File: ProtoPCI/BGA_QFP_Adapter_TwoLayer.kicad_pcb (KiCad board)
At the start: 2 copper layers, 30.2 x 30.2 mm, 2 parts

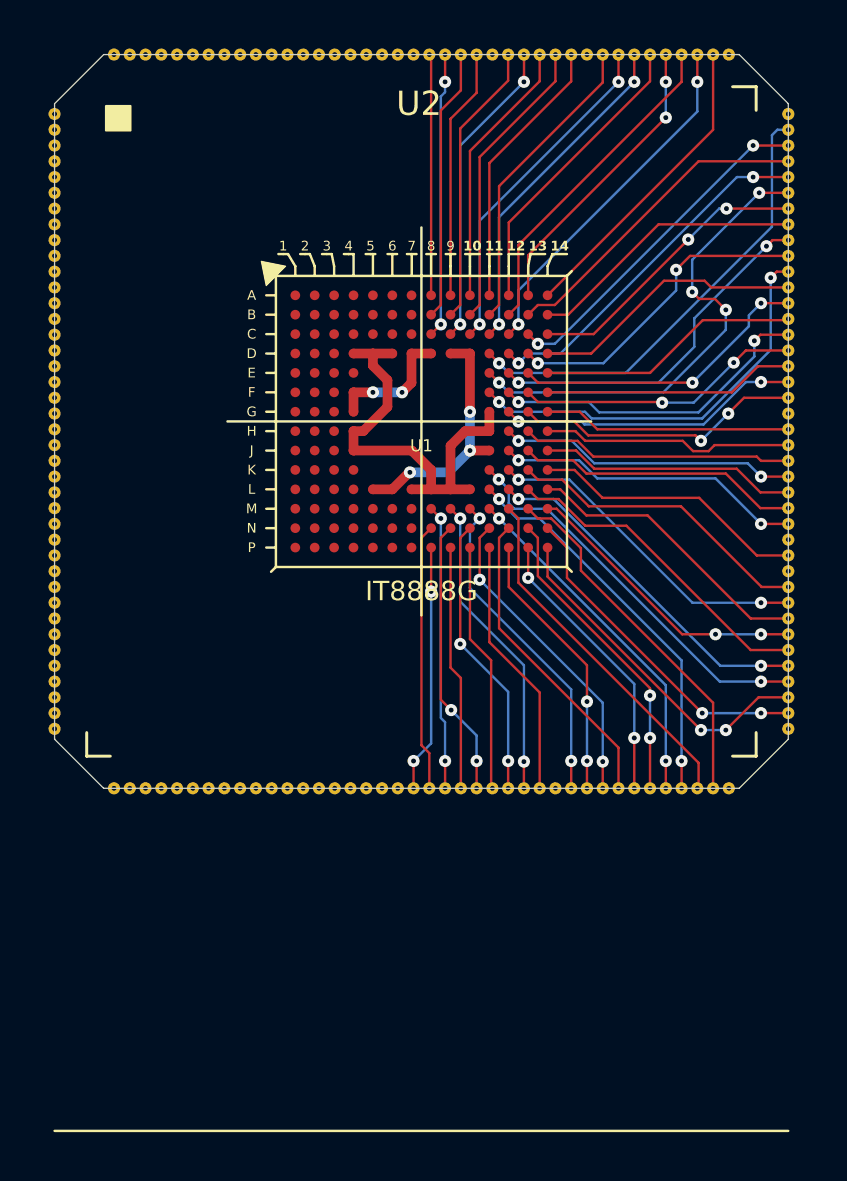
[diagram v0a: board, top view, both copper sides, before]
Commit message: BGA/QFP Adapter Two Layer Baseline
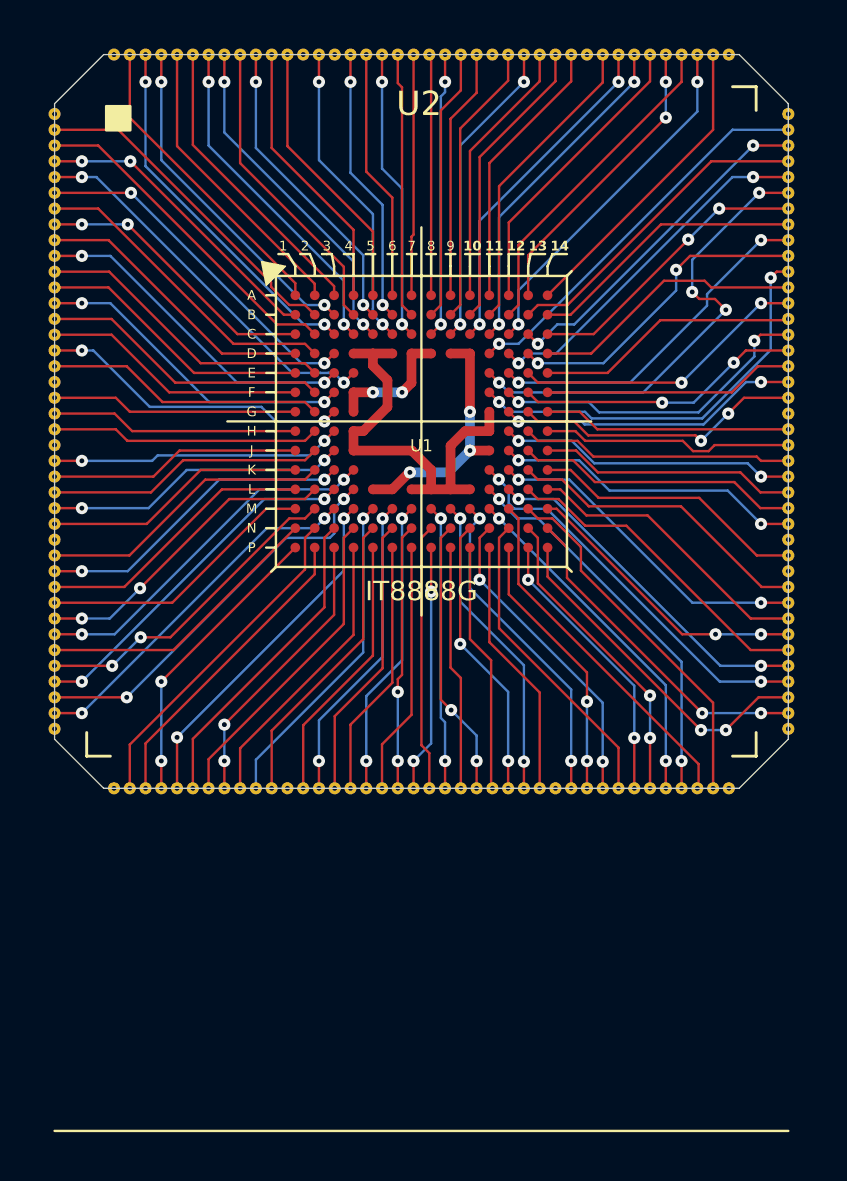
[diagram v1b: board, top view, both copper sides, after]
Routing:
- net Net-(U1-DACK5#): track 0.00 -> 16.4 mm, vias 0 -> 2
- net Net-(U1-TRDY#): track 0.00 -> 16.0 mm, vias 0 -> 2
- net Net-(U1-AD17): track 0.00 -> 15.2 mm, vias 0 -> 2
- net Net-(U1-SCLK): track 0.00 -> 15.1 mm, vias 0 -> 2
- net Net-(U1-DACK3#): track 0.00 -> 15.0 mm, vias 0 -> 2
- net Net-(U1-DACK6#): track 0.00 -> 14.8 mm, vias 0 -> 2
- net Net-(U1-DEVSEL#): track 0.00 -> 14.5 mm, vias 0 -> 2
- net Net-(U1-DRQ7): track 0.00 -> 14.5 mm, vias 0 -> 2
- net Net-(U1-AD18): track 0.00 -> 14.1 mm, vias 0 -> 2
- net Net-(U1-AD22): track 0.00 -> 14.0 mm, vias 0 -> 2
- net Net-(U1-AD21): track 0.00 -> 13.9 mm, vias 0 -> 2
- net Net-(U1-C/BE2#): track 0.00 -> 13.9 mm
- net Net-(U1-FRAME#): track 0.00 -> 13.9 mm
- net Net-(U1-DACK2#): track 0.00 -> 13.8 mm
- net Net-(U1-SERR#): track 0.00 -> 13.8 mm, vias 0 -> 2
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
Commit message: Finalized BGA/QFP Adapter (TwoLayer File *4LayerActual)
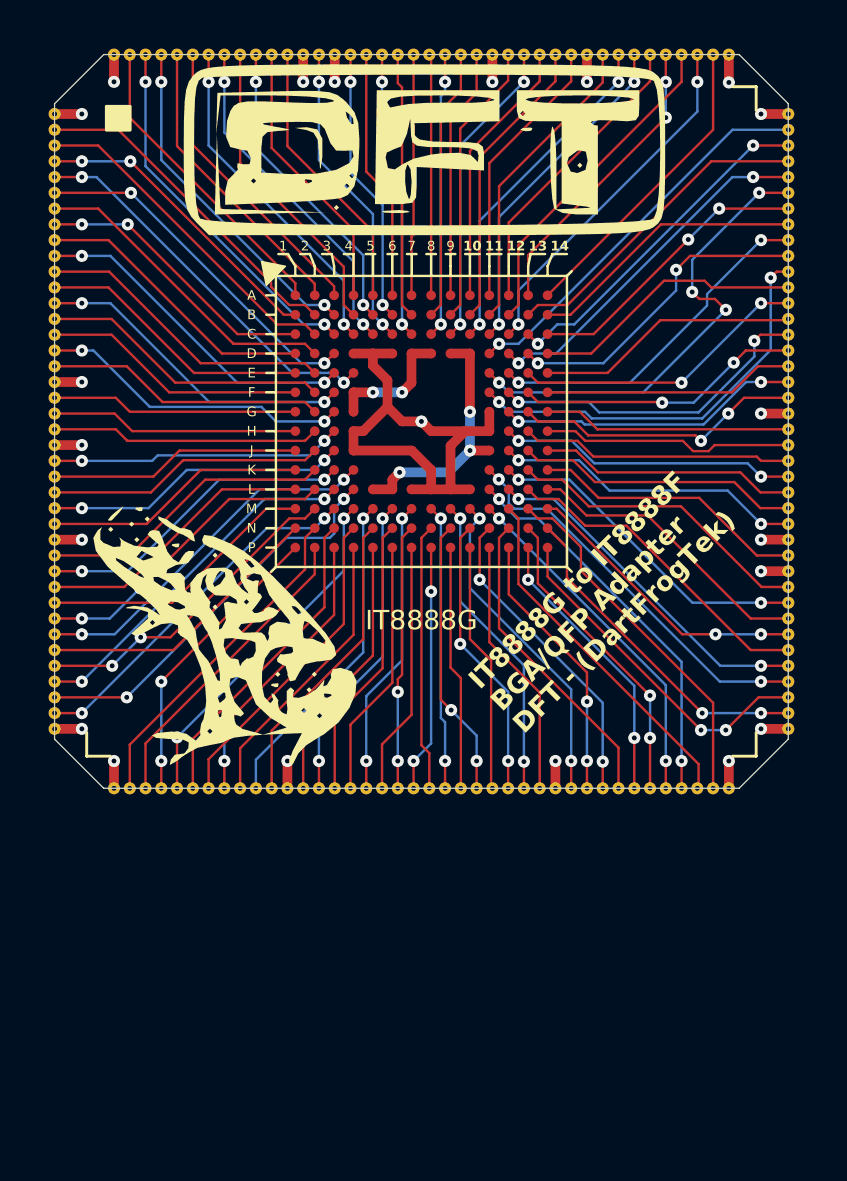
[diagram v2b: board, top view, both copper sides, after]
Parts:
- added G***: LOGO, ISA8888:DFT_Logo_Tiny, F.Cu at (166.7, 104.2)
- added G***: LOGO, ISA8888:DF_SS_Tiny, F.Cu at (158.5, 124.3)
- added G***: LOGO, ISA8888:DFT_SS_Small, B.Cu at (166.7, 115.0)
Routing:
- net /GND: track 17.9 -> 194.0 mm, vias 0 -> 13
- net /VCC: track 10.3 -> 83.9 mm, vias 3 -> 7
- net /VCC3: track 5.37 -> 61.9 mm, vias 2 -> 6
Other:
- copper layers 2 -> 4
- board text added: "IT8888G to IT8888F BGA/QFP Adapter DFT - (DartFrogTek)"
